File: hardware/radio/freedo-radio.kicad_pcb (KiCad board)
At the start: 2 copper layers, 0 parts

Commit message: feat(hardware): set up the board stackup, rules and outline
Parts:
- added BR401: MB10S, freedo-radio:MBS_L4.7-W3.8-P2.40-LS7.0-TL, F.Cu at (166.6, 100.5)
- added BR402: MB10S, freedo-radio:MBS_L4.7-W3.8-P2.40-LS7.0-TL, F.Cu at (166.6, 106.8)
- added C1: 1uF, freedo-radio:C_0402_1005Metric, F.Cu at (143.4, 117.8)
- added C101: 15pF, freedo-radio:C_0402_1005Metric, F.Cu at (143.4, 127.7)
- added C111: 100nF, freedo-radio:C_0402_1005Metric, F.Cu at (143.4, 129.6)
- added C121: 1pF, freedo-radio:C_0402_1005Metric, F.Cu at (146.3, 117.8)
- added C122: 1.5pF, freedo-radio:C_0402_1005Metric, F.Cu at (146.3, 119.8)
- added C123: 3.3pF, freedo-radio:C_0402_1005Metric, F.Cu at (146.3, 121.8)
- added C124: 100pF, freedo-radio:C_0402_1005Metric, F.Cu at (146.3, 123.7)
- added C125: 12pF, freedo-radio:C_0402_1005Metric, F.Cu at (146.3, 125.7)
- added C126: 47pF, freedo-radio:C_0402_1005Metric, F.Cu at (146.3, 127.7)
- added C131: 1.5pF, freedo-radio:C_0402_1005Metric, F.Cu at (146.3, 129.6)
- added C141: 100nF, freedo-radio:C_0402_1005Metric, F.Cu at (149.1, 117.8)
- added C151: 100nF, freedo-radio:C_0402_1005Metric, F.Cu at (149.1, 119.8)
- added C181: 100nF, freedo-radio:C_0402_1005Metric, F.Cu at (149.1, 121.8)
- added C191: DNP, freedo-radio:C_0402_1005Metric, F.Cu at (149.1, 123.7)
- added C192: DNP, freedo-radio:C_0402_1005Metric, F.Cu at (149.1, 125.7)
- added C201: 1uF, freedo-radio:C_0603_1608Metric, F.Cu at (103.5, 106.6)
- added C202: 22uF, freedo-radio:C_0805_2012Metric, F.Cu at (112.4, 135.7)
- added C203: 100nF, freedo-radio:C_0603_1608Metric, F.Cu at (95.5, 121.3)
- added C204: 10uF, freedo-radio:C_0603_1608Metric, F.Cu at (95.5, 123.8)
- added C205: 100nF, freedo-radio:C_0603_1608Metric, F.Cu at (95.5, 126.3)
- added C206: 22uF, freedo-radio:C_0603_1608Metric, F.Cu at (103.5, 109.1)
- added C207: 100nF, freedo-radio:C_0603_1608Metric, F.Cu at (103.5, 111.6)
- added C208: 100nF, freedo-radio:C_0603_1608Metric, F.Cu at (95.5, 128.8)
- added C301: 18pF, freedo-radio:C_0603_1608Metric, F.Cu at (144.0, 70.3)
- added C302: 18pF, freedo-radio:C_0603_1608Metric, F.Cu at (144.0, 72.8)
- added C303: 4.7uF, freedo-radio:C_0603_1608Metric, F.Cu at (144.0, 75.3)
- added C304: 10nF, freedo-radio:C_0603_1608Metric, F.Cu at (144.0, 77.8)
- added C305: 100nF, freedo-radio:C_0603_1608Metric, F.Cu at (144.0, 80.3)
- added C306: 100nF, freedo-radio:C_0603_1608Metric, F.Cu at (144.0, 82.8)
- added C307: 100nF, freedo-radio:C_0603_1608Metric, F.Cu at (144.0, 85.3)
- added C308: 100nF, freedo-radio:C_0603_1608Metric, F.Cu at (144.0, 87.8)
- added C309: 100nF, freedo-radio:C_0603_1608Metric, F.Cu at (144.0, 90.3)
- added C310: 100nF, freedo-radio:C_0603_1608Metric, F.Cu at (148.0, 70.3)
- added C311: 10uF, freedo-radio:C_0603_1608Metric, F.Cu at (148.0, 72.8)
- added C312: 10uF, freedo-radio:C_0603_1608Metric, F.Cu at (148.0, 75.3)
- added C313: 100nF, freedo-radio:C_0603_1608Metric, F.Cu at (148.0, 77.8)
- added C314: 22nF, freedo-radio:C_0603_1608Metric, F.Cu at (148.0, 80.3)
- added C315: 6.8nF, freedo-radio:C_0603_1608Metric, F.Cu at (148.0, 82.8)
- added C316: 6.8nF, freedo-radio:C_0603_1608Metric, F.Cu at (148.0, 85.3)
- added C317: 10nF, freedo-radio:C_0603_1608Metric, F.Cu at (148.0, 87.8)
- added C318: 10nF/100V, freedo-radio:C_0603_1608Metric, F.Cu at (148.0, 90.3)
- added C319: 10nF/100V, freedo-radio:C_0603_1608Metric, F.Cu at (152.0, 70.3)
- added C320: 10nF/100V, freedo-radio:C_0603_1608Metric, F.Cu at (152.0, 72.8)
- added C321: 10nF/100V, freedo-radio:C_0603_1608Metric, F.Cu at (152.0, 75.3)
- added C322: 1nF/2kV, freedo-radio:C_1808_4520Metric, F.Cu at (182.2, 107.5)
- added C323: 1nF/2kV, freedo-radio:C_1808_4520Metric, F.Cu at (182.2, 111.3)
- added C401: 100uF, freedo-radio:CP_Elec_6.3x7.7, F.Cu at (176.4, 101.5)
- added C402: 10uF, freedo-radio:C_0805_2012Metric, F.Cu at (183.9, 103.7)
- added C41: 100nF, freedo-radio:C_0402_1005Metric, F.Cu at (143.4, 119.8)
- added C51: 100nF, freedo-radio:C_0402_1005Metric, F.Cu at (143.4, 121.8)
- added C81: 15pF, freedo-radio:C_0402_1005Metric, F.Cu at (143.4, 123.7)
- added C91: 100nF, freedo-radio:C_0402_1005Metric, F.Cu at (143.4, 125.7)
- added D201: SMF5.0A, freedo-radio:SOD-123FL_L2.7-W1.8-LS3.8-RD, F.Cu at (111.7, 121.5)
- added D202: SS34, freedo-radio:SMA_L4.3-W2.6-LS5.2-RD, F.Cu at (104.8, 139.6)
- added D203: KT-0603R, freedo-radio:LED_0603_1608Metric, F.Cu at (123.7, 106.6)
- added D204: KT-0603R, freedo-radio:LED_0603_1608Metric, F.Cu at (123.7, 109.2)
- added D205: KT-0603R, freedo-radio:LED_0603_1608Metric, F.Cu at (123.7, 111.8)
- added D206: KT-0603R, freedo-radio:LED_0603_1608Metric, F.Cu at (123.7, 114.4)
- added D301: KT-0603R, freedo-radio:LED_0603_1608Metric, F.Cu at (186.8, 70.3)
- added D302: KT-0603R, freedo-radio:LED_0603_1608Metric, F.Cu at (186.8, 72.9)
- added D401: SMAJ58A, freedo-radio:SMA_L4.3-W2.6-LS5.2-RD, F.Cu at (174.9, 107.6)
- added D402: SS34, freedo-radio:SMA_L4.3-W2.6-LS5.2-RD, F.Cu at (174.9, 111.6)
- added F201: BSMD0805-075-16V, freedo-radio:F0805, F.Cu at (111.6, 124.6)
- added FB301: BLM18PG121SN1D, freedo-radio:L_0603_1608Metric, F.Cu at (152.0, 77.8)
- added H1: MountingHole_3.2mm_M3, freedo-radio:MountingHole_3.2mm_M3, F.Cu at (194.0, 54.0)
- added H2: MountingHole_3.2mm_M3, freedo-radio:MountingHole_3.2mm_M3, F.Cu at (278.0, 54.0)
- added H3: MountingHole_3.2mm_M3, freedo-radio:MountingHole_3.2mm_M3, F.Cu at (194.0, 106.0)
- added H4: MountingHole_3.2mm_M3, freedo-radio:MountingHole_3.2mm_M3, F.Cu at (278.0, 106.0)
- added J1: SMA-KE-347-H13.5-1.6, freedo-radio:SMA_XUNPU_SMA-KE-347-H13.5-1.6_EdgeMount, F.Cu at (154.8, 119.7)
- added J201: TYPE-C-31-M-12, freedo-radio:HRO_TYPE-C-31-M-12, F.Cu at (103.2, 123.9)
- added J202: UART0, freedo-radio:PinHeader_1x04_P2.54mm_Vertical, F.Cu at (115.8, 107.6)
- added J301: DS1128-S80BP, freedo-radio:RJ45_CONNFLY_DS1128-S80BP, F.Cu at (151.7, 100.5)
- added L1: BLM15HG102SN1D, freedo-radio:L_0402_1005Metric, F.Cu at (143.4, 131.6)
- added L121: 12nH, freedo-radio:L_0402_1005Metric, F.Cu at (143.4, 133.6)
- added L122: 18nH, freedo-radio:L_0402_1005Metric, F.Cu at (143.4, 135.6)
- added L123: 12nH, freedo-radio:L_0402_1005Metric, F.Cu at (143.4, 137.6)
- added L124: 12nH, freedo-radio:L_0402_1005Metric, F.Cu at (143.4, 139.6)
- added L125: 3.3nH, freedo-radio:L_0402_1005Metric, F.Cu at (146.3, 131.6)
- added L131: 12nH, freedo-radio:L_0402_1005Metric, F.Cu at (146.3, 133.6)
- added L132: 18nH, freedo-radio:L_0402_1005Metric, F.Cu at (146.3, 135.6)
- added R171: 56k, freedo-radio:R_0402_1005Metric, F.Cu at (146.3, 137.6)
- added R191: 0R, freedo-radio:R_0402_1005Metric, F.Cu at (146.3, 139.6)
- added R201: 5.1k, freedo-radio:R_0603_1608Metric, F.Cu at (95.5, 131.3)
- added R202: 5.1k, freedo-radio:R_0603_1608Metric, F.Cu at (95.5, 133.8)
- added R203: 22R, freedo-radio:R_0603_1608Metric, F.Cu at (103.5, 114.1)
- added R204: 22R, freedo-radio:R_0603_1608Metric, F.Cu at (103.5, 116.6)
- added R205: 10k, freedo-radio:R_0603_1608Metric, F.Cu at (107.5, 106.6)
- added R206: 10k, freedo-radio:R_0603_1608Metric, F.Cu at (107.5, 109.1)
- added R207: 510R, freedo-radio:R_0603_1608Metric, F.Cu at (107.5, 111.6)
- added R208: 33R, freedo-radio:R_0603_1608Metric, F.Cu at (107.5, 114.1)
- added R209: 33R, freedo-radio:R_0603_1608Metric, F.Cu at (107.5, 116.6)
- added R210: 10k, freedo-radio:R_0603_1608Metric, F.Cu at (159.0, 138.0)
- added R211: 1k, freedo-radio:R_0603_1608Metric, F.Cu at (111.5, 106.6)
- added R212: 1k, freedo-radio:R_0603_1608Metric, F.Cu at (111.5, 109.1)
- added R213: 1k, freedo-radio:R_0603_1608Metric, F.Cu at (111.5, 111.6)
- added R214: 1k, freedo-radio:R_0603_1608Metric, F.Cu at (111.5, 114.1)
- added R215: 10k, freedo-radio:R_0603_1608Metric, F.Cu at (95.5, 136.3)
- added R301: 1M, freedo-radio:R_0603_1608Metric, F.Cu at (152.0, 80.3)
- added R302: 0R, freedo-radio:R_0603_1608Metric, F.Cu at (152.0, 82.8)
- added R303: 12.4k, freedo-radio:R_0603_1608Metric, F.Cu at (152.0, 85.3)
- added R304: 49.9R, freedo-radio:R_0603_1608Metric, F.Cu at (152.0, 87.8)
- added R305: 49.9R, freedo-radio:R_0603_1608Metric, F.Cu at (152.0, 90.3)
- added R306: 10R, freedo-radio:R_0603_1608Metric, F.Cu at (156.0, 70.3)
- added R307: 82R, freedo-radio:R_0603_1608Metric, F.Cu at (156.0, 72.8)
- added R308: 82R, freedo-radio:R_0603_1608Metric, F.Cu at (156.0, 75.3)
- added R309: 0R, freedo-radio:R_0603_1608Metric, F.Cu at (156.0, 77.8)
- added R310: 0R, freedo-radio:R_0603_1608Metric, F.Cu at (156.0, 80.3)
- added R311: 0R, freedo-radio:R_0603_1608Metric, F.Cu at (156.0, 82.8)
- added R312: 0R, freedo-radio:R_0603_1608Metric, F.Cu at (156.0, 85.3)
- added R313: 10k, freedo-radio:R_0603_1608Metric, F.Cu at (156.0, 87.8)
- added R314: 10k, freedo-radio:R_0603_1608Metric, F.Cu at (156.0, 90.3)
- added R315: 1k, freedo-radio:R_0603_1608Metric, F.Cu at (160.0, 70.3)
- added R316: 1k, freedo-radio:R_0603_1608Metric, F.Cu at (160.0, 72.8)
- added R317: 75R, freedo-radio:R_0603_1608Metric, F.Cu at (160.0, 75.3)
- added R318: 75R, freedo-radio:R_0603_1608Metric, F.Cu at (160.0, 77.8)
- added R319: 75R, freedo-radio:R_0603_1608Metric, F.Cu at (160.0, 80.3)
- added R320: 75R, freedo-radio:R_0603_1608Metric, F.Cu at (160.0, 82.8)
- added R401: 0R, freedo-radio:R_0603_1608Metric, F.Cu at (160.0, 85.3)
- added R402: 56R, freedo-radio:R_2512_6332Metric, F.Cu at (166.4, 112.4)
- added SW201: TS-1187A-B-A-B, freedo-radio:SW_XKB_TS-1187A, F.Cu at (97.5, 108.5)
- added SW202: TS-1187A-B-A-B, freedo-radio:SW_XKB_TS-1187A, F.Cu at (97.5, 114.8)
- added T301: B1608S, freedo-radio:CND-tek_B1608S_SMD-16_P1.27mm, F.Cu at (169.1, 91.4)
- added TP101: CC_SCK, freedo-radio:TestPoint_Pad_D1.5mm, F.Cu at (160.9, 118.6)
- added TP102: CC_MOSI, freedo-radio:TestPoint_Pad_D1.5mm, F.Cu at (160.9, 122.2)
- added TP103: CC_MISO, freedo-radio:TestPoint_Pad_D1.5mm, F.Cu at (160.9, 125.7)
- added TP104: CC_CSN, freedo-radio:TestPoint_Pad_D1.5mm, F.Cu at (160.9, 129.3)
- added TP105: CC_GDO0, freedo-radio:TestPoint_Pad_D1.5mm, F.Cu at (164.4, 118.6)
- added TP106: CC_GDO2, freedo-radio:TestPoint_Pad_D1.5mm, F.Cu at (164.4, 122.2)
- added TP107: GND, freedo-radio:TestPoint_Pad_D1.5mm, F.Cu at (164.4, 125.7)
- added TP211: UART0_TX, freedo-radio:TestPoint_Pad_D1.5mm, F.Cu at (119.9, 107.1)
- added TP212: UART0_RX, freedo-radio:TestPoint_Pad_D1.5mm, F.Cu at (119.9, 110.6)
- added TP213: GND, freedo-radio:TestPoint_Pad_D1.5mm, F.Cu at (119.9, 114.2)
- added TP250: 5V_SYS, freedo-radio:TestPoint_Pad_D1.5mm, F.Cu at (99.3, 131.6)
- added TP251: 3V3, freedo-radio:TestPoint_Pad_D1.5mm, F.Cu at (99.3, 135.1)
- added TP252: GND, freedo-radio:TestPoint_Pad_D1.5mm, F.Cu at (99.3, 138.7)
- added TP301: GND, freedo-radio:TestPoint_Pad_D1.5mm, F.Cu at (186.5, 76.0)
- added U1: CC1101RGPR, freedo-radio:QFN-20-1EP_4x4mm_P0.5mm_EP2.4x2.4mm_TI_RGP0020H, F.Cu at (154.0, 135.0)
- added U201: ESP32-S3-MINI-1-N8, freedo-radio:ESP32-S3-MINI-1, F.Cu at (116.7, 94.3)
- added U202: USBLC6-2SC6, freedo-radio:SOT-23-6_L2.9-W1.6-P0.95-LS2.8-BL, F.Cu at (112.7, 132.0)
- added U203: LDL1117S33R, freedo-radio:SOT-223-4_L6.5-W3.5-P2.30-LS7.0-BR, F.Cu at (105.6, 133.7)
- added U301: W5500, freedo-radio:LQFP-48_L7.0-W7.0-P0.50-LS9.0-BL, F.Cu at (181.8, 91.0)
- added U401: DP9900LP-5V, freedo-radio:SDAPO_DP9900LP_THT-8, F.Cu at (173.4, 76.8)
- added X1: X322526MMB4SI, freedo-radio:CRYSTAL-SMD_4P-L3.2-W2.5-BL, F.Cu at (159.8, 134.2)
- added Y301: X322525MOB4SI, freedo-radio:CRYSTAL-SMD_4P-L3.2-W2.5-BL, F.Cu at (184.5, 99.7)
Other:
- board outline added: 92 x 60 mm
- copper layers 2 -> 4
- board text added: "Barrier: no copper"
- board text added: "Ethernet U301"
- board text added: "Line side"
- board text added: "MCU U201"
- board text added: "MCU support"
- board text added: "Power U203"
- board text added: "RF U1 / J1"
- board text added: "SHIELD"
- board text added: "U201 antenna overhang"
- board text added: "USB J201"

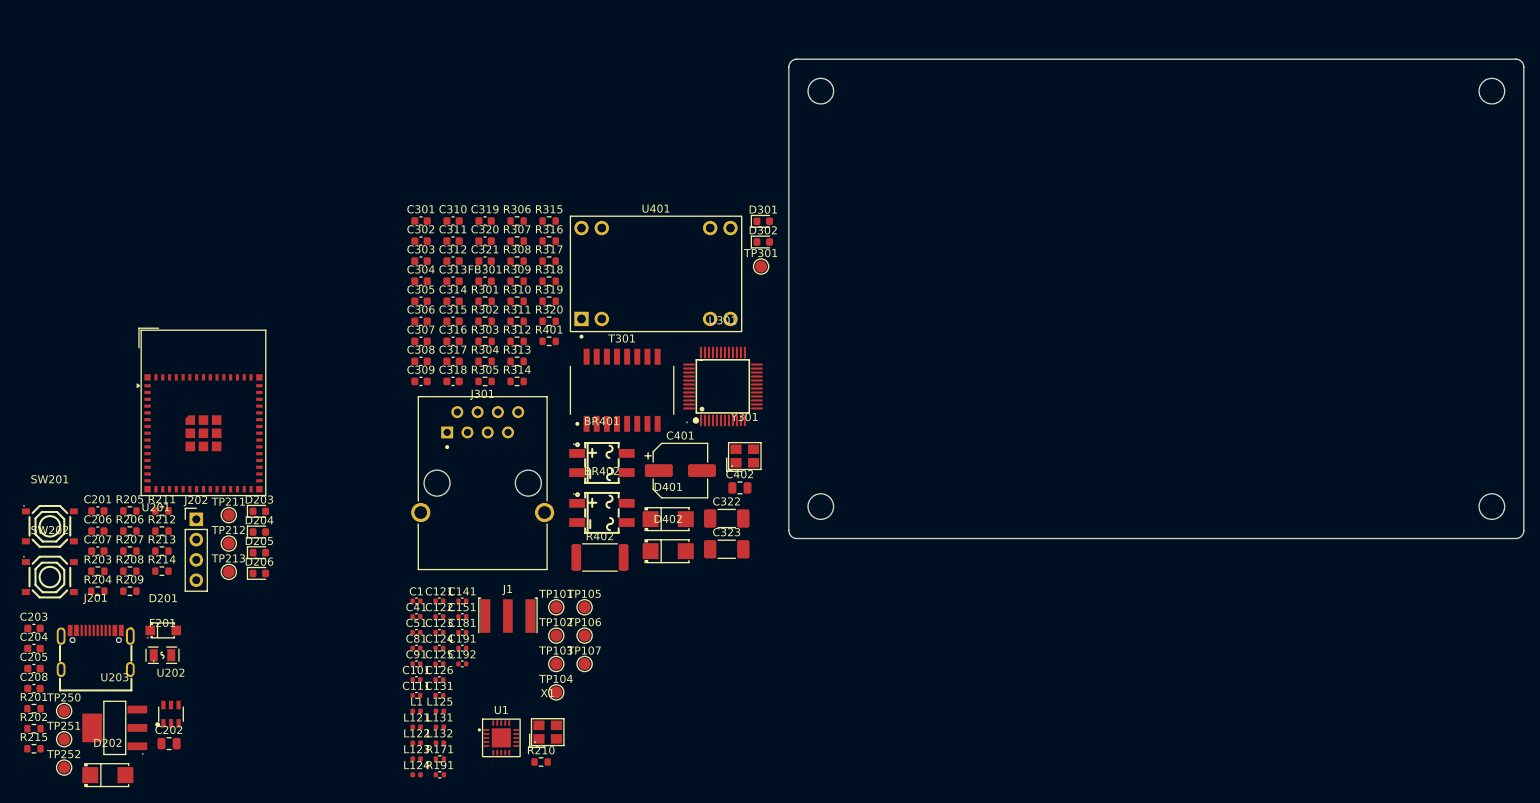
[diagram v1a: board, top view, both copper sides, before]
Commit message: feat(hardware): place the rev a footprints
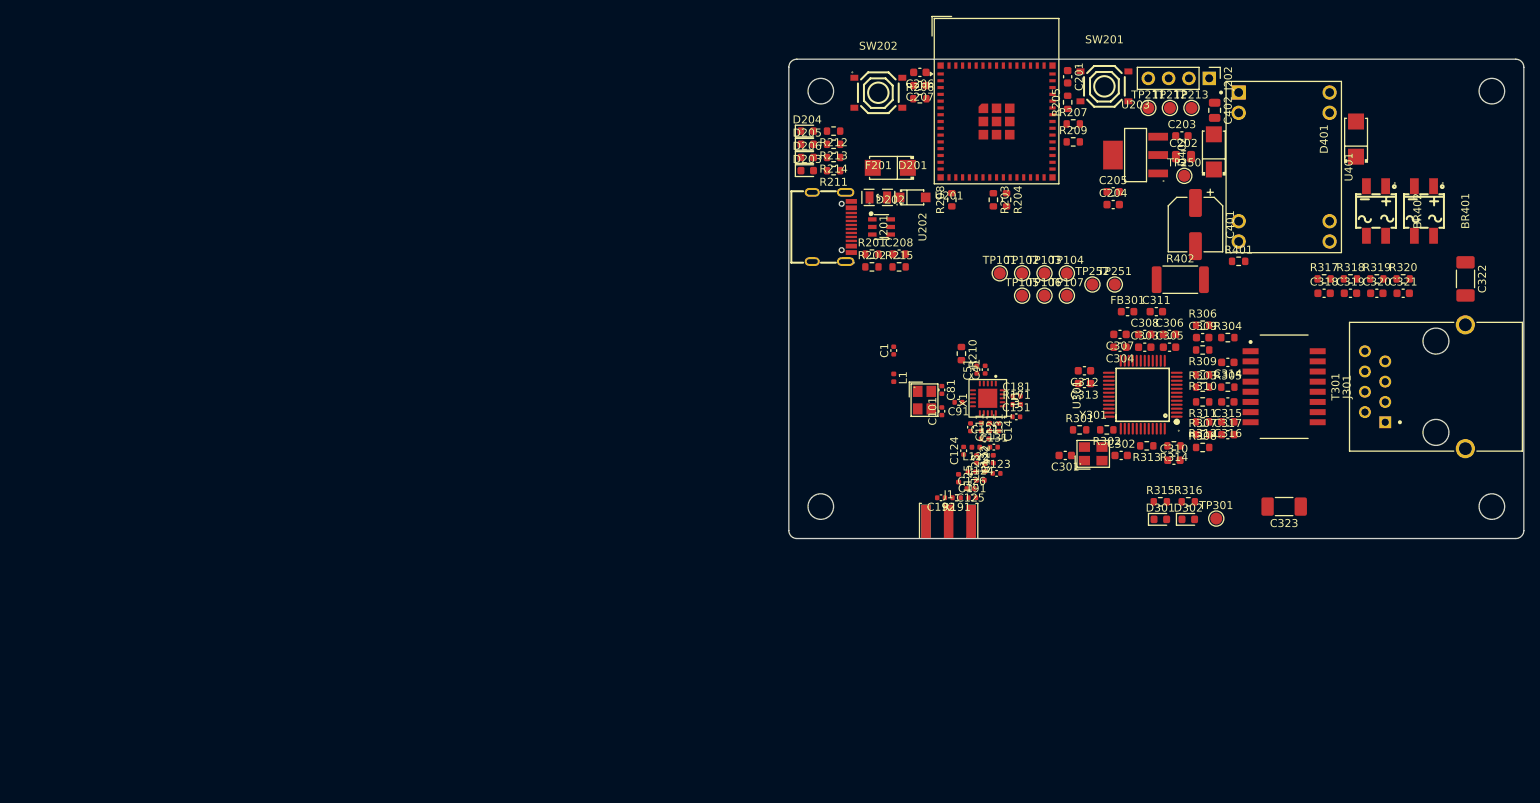
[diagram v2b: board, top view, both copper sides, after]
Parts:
- moved C203 156.4 mm to (239.2, 59.6)
- moved TP250 155.4 mm to (239.5, 64.6)
- moved C205 147.7 mm to (230.6, 66.6)
- moved C202 146.7 mm to (239.4, 62.2)
- moved U203 146.5 mm to (233.4, 62.0)
- moved C204 146.1 mm to (230.6, 68.2)
- moved TP251 143.3 mm to (230.8, 78.2)
- moved SW201 143.0 mm to (229.5, 53.4)
- moved TP252 142.2 mm to (228.0, 78.2)
- moved J202 138.3 mm to (242.6, 52.4), turned to -90 degrees
- moved TP213 133.8 mm to (240.4, 56.1)
- moved C201 133.0 mm to (224.9, 52.2), turned to -90 degrees
- moved R209 130.8 mm to (225.6, 60.4)
- moved TP212 129.8 mm to (237.7, 56.1)
- moved R207 129.6 mm to (225.6, 58.1)
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
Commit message: feat(hardware): route the critical nets and ground planes
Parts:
- moved C309 7.19 mm to (238.7, 91.3)
- moved R306 6.92 mm to (248.6, 82.0), turned to 180 degrees
- moved C310 6.72 mm to (238.7, 93.5)
- moved R317 6.67 mm to (263.5, 76.0), turned to -90 degrees
- moved C318 6.50 mm to (263.5, 79.1), turned to -90 degrees
- moved R319 6.09 mm to (269.5, 76.0), turned to -90 degrees
- moved C320 5.90 mm to (269.5, 79.1), turned to -90 degrees
- moved C314 5.68 mm to (248.6, 83.6), turned to 0 degrees
- moved C1 5.28 mm to (203.1, 91.8), turned to -90 degrees
- moved C306 3.94 mm to (238.7, 88.2)
- moved R307 3.65 mm to (241.9, 93.3), turned to 180 degrees
- moved R308 3.65 mm to (241.9, 95.0)
- moved R310 3.10 mm to (244.9, 89.1)
- moved R309 3.07 mm to (244.9, 86.6)
- moved R303 2.86 mm to (239.2, 89.8)
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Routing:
- net +3V3: track 0.00 -> 143.9 mm, vias 0 -> 18
- net /ethernet_poe/3V3A: track 0.00 -> 77.3 mm, vias 0 -> 5
- net GND: track 0.00 -> 74.0 mm, vias 0 -> 198
- net /rf/3V3_RF: track 0.00 -> 52.3 mm, vias 0 -> 8
- net /ethernet_poe/5V_SYS: track 0.00 -> 49.2 mm, vias 0 -> 2
- net /ethernet_poe/SHIELD: track 0.00 -> 48.3 mm
- net /ethernet_poe/+VDC: track 0.00 -> 37.5 mm
- net /ethernet_poe/CT_36: track 0.00 -> 28.0 mm, vias 0 -> 2
- net /ethernet_poe/VIN-: track 0.00 -> 27.8 mm, vias 0 -> 3
- net /ethernet_poe/PAIR_45: track 0.00 -> 26.7 mm, vias 0 -> 1
- net /ethernet_poe/VIN+: track 0.00 -> 26.4 mm
- net /ethernet_poe/BS: track 0.00 -> 23.7 mm
- net /usb_power/USB_DN: track 0.00 -> 22.6 mm
- net /usb_power/USB_DP: track 0.00 -> 22.6 mm
- net /ethernet_poe/PAIR_78: track 0.00 -> 22.5 mm, vias 0 -> 1
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- added copper zone on B.Cu, net +3V3
- added copper zone on F.Cu, net +3V3
- added copper zone on B.Cu, net GND
- added copper zone on F.Cu, net GND
- added copper zone on In1.Cu, net GND
- added copper zone on In2.Cu, net GND

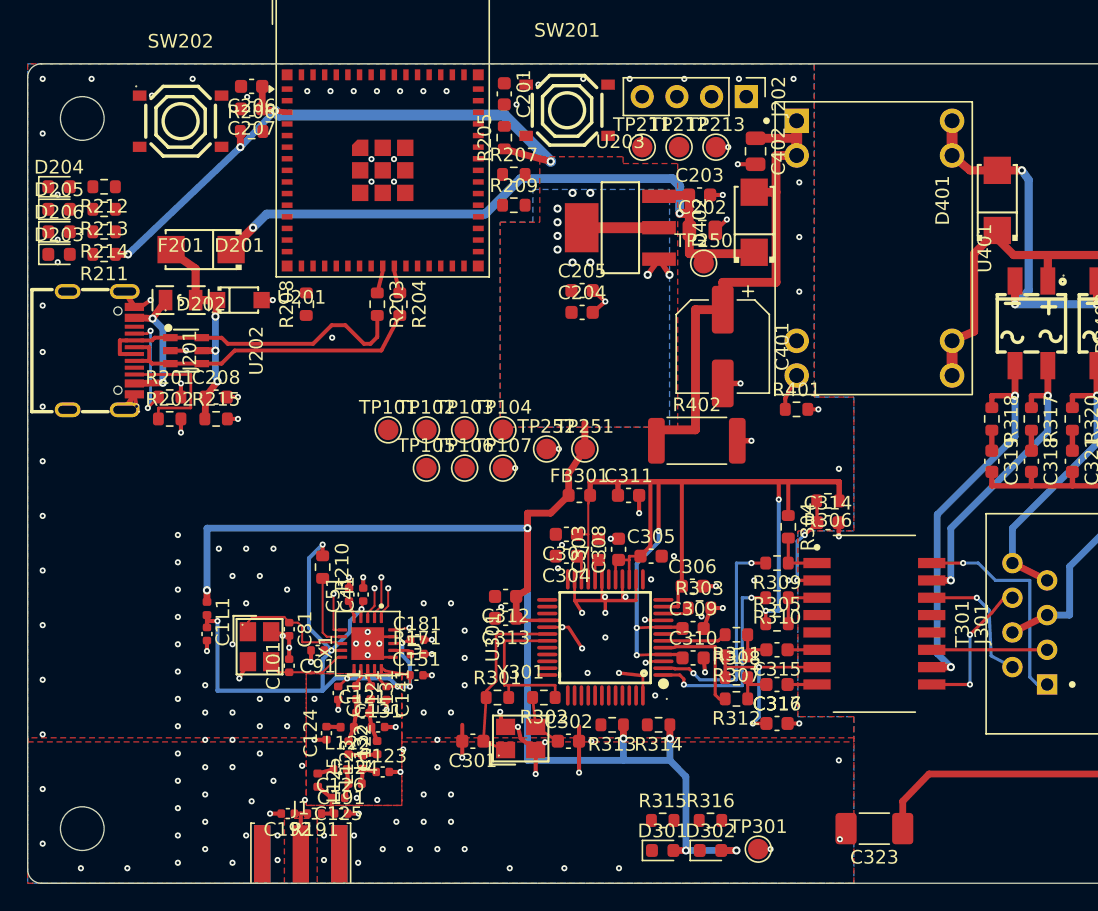
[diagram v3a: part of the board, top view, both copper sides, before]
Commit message: feat(hardware): route the remaining nets and close drc
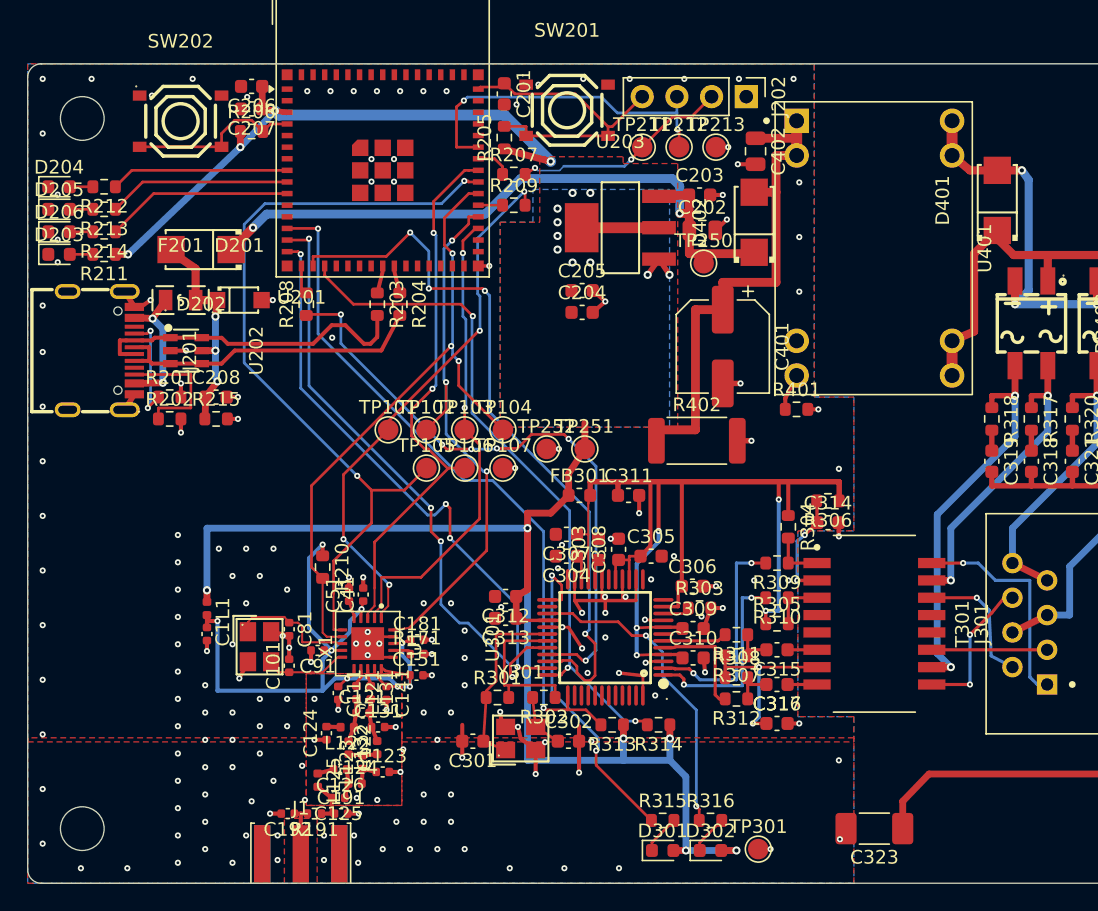
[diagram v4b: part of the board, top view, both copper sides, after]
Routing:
- net /mcu/CC_GDO0: track 3.15 -> 58.5 mm, vias 1 -> 2
- net /ethernet_poe/ETH_MISO: track 0.00 -> 53.7 mm, vias 0 -> 4
- net /ethernet_poe/ETH_RST: track 0.00 -> 51.2 mm, vias 0 -> 2
- net /ethernet_poe/ETH_INT: track 0.00 -> 50.8 mm, vias 0 -> 3
- net /ethernet_poe/ETH_SCK: track 0.00 -> 45.5 mm, vias 0 -> 6
- net /ethernet_poe/ETH_CS: track 0.00 -> 44.5 mm, vias 0 -> 4
- net /mcu/CC_CSN: track 5.40 -> 47.6 mm, vias 0 -> 3
- net /ethernet_poe/ETH_MOSI: track 0.00 -> 42.0 mm, vias 0 -> 4
- net /mcu/CC_MOSI: track 1.06 -> 40.6 mm, vias 1 -> 3
- net /mcu/CC_GDO2: track 2.21 -> 40.5 mm, vias 1 -> 2
- net /mcu/CC_SCK: track 2.21 -> 39.6 mm, vias 1 -> 4
- net /mcu/CC_MISO: track 3.01 -> 34.6 mm, vias 1 -> 2
- net /mcu/UART0_RX: track 0.00 -> 25.2 mm, vias 0 -> 2
- net Net-(U301-LINKLED): track 0.00 -> 24.2 mm, vias 0 -> 2
- net /mcu/EN: track 0.00 -> 23.4 mm
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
